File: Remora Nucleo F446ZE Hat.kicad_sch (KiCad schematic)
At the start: 5 parts, among them J1 NucleoF446ZE CN11 Header, J2 NucleoF446ZE CN12 Header

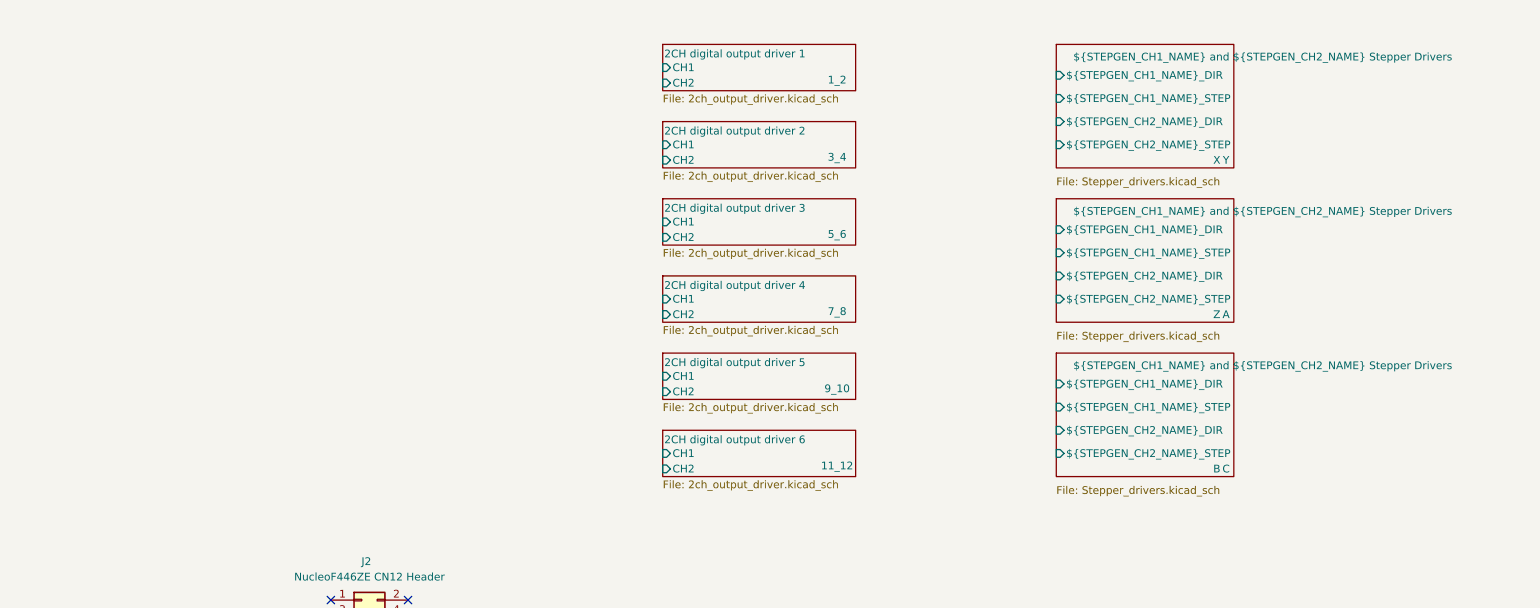
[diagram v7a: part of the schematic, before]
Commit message: Completed design for digital outputs, tidied into own sheets and bussing for scalability
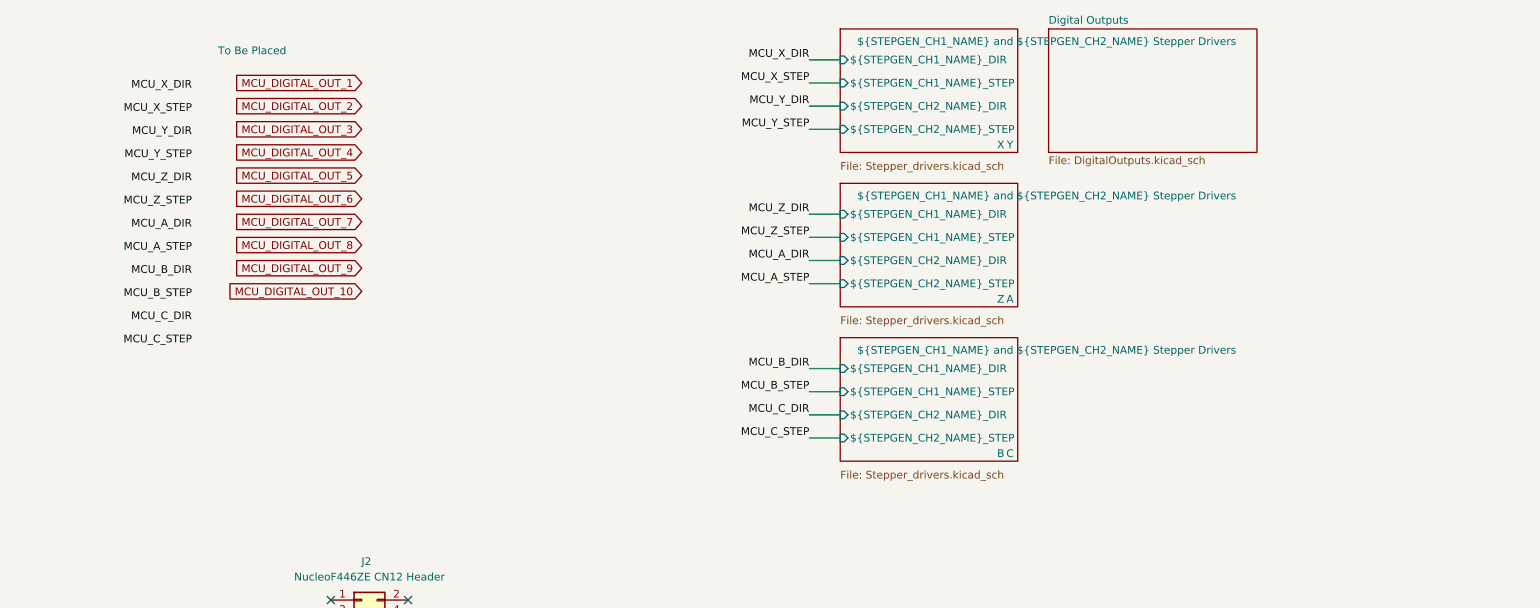
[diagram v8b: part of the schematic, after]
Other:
- removed sheet 2CH digital output driver 1
- removed sheet 2CH digital output driver 2
- removed sheet 2CH digital output driver 3
- removed sheet 2CH digital output driver 4
- removed sheet 2CH digital output driver 5
- removed sheet 2CH digital output driver 6
- added sheet Digital Outputs (DigitalOutputs.kicad_sch)
- note added: "To Be Placed"
